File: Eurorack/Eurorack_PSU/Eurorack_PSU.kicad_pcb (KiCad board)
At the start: 2 copper layers, 95 x 58 mm, 20 parts, among them J1 AC, J2 AC, U1 LM7812_TO220, U2 LM7912_TO220

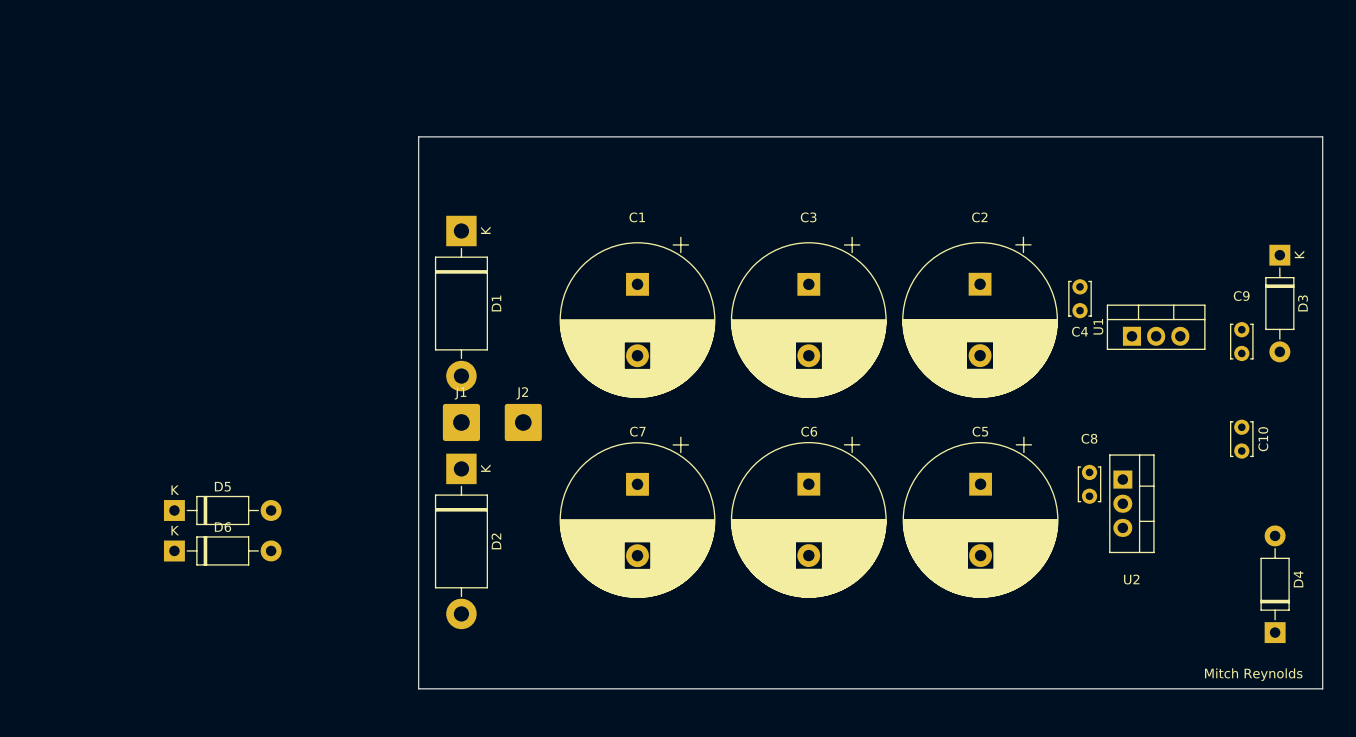
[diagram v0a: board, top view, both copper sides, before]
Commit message: Update PSU and add more spice models
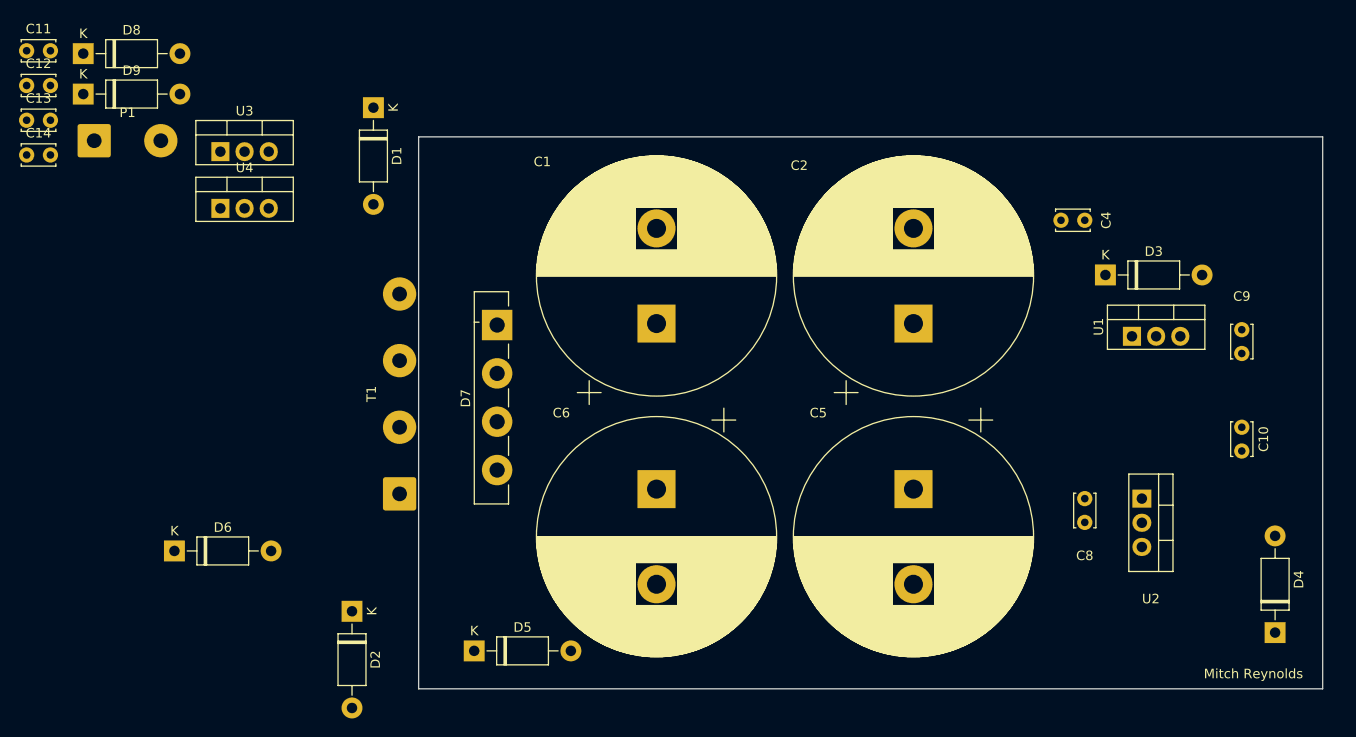
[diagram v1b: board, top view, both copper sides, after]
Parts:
- removed C3, C7: 2200uF 25v, Capacitor_THT:CP_Radial_D16.0mm_P7.50mm
- removed J1, J2: AC, Connector_Wire:SolderWire-1sqmm_1x01_D1.4mm_OD3.9mm
- added C11: 1uF, Capacitor_THT:C_Disc_D3.4mm_W2.1mm_P2.50mm, F.Cu at (14.8, 25.9)
- added C12: 1uF, Capacitor_THT:C_Disc_D3.4mm_W2.1mm_P2.50mm, F.Cu at (14.8, 29.6)
- added C13: 1uF, Capacitor_THT:C_Disc_D3.4mm_W2.1mm_P2.50mm, F.Cu at (14.8, 33.2)
- added C14: 1uF, Capacitor_THT:C_Disc_D3.4mm_W2.1mm_P2.50mm, F.Cu at (14.8, 36.9)
- added D7: GBU6A, Diode_THT:Diode_Bridge_Vishay_GBU, F.Cu at (64.2, 54.8)
- added D8: 1N4007, Diode_THT:D_DO-41_SOD81_P10.16mm_Horizontal, F.Cu at (20.8, 26.2)
- added D9: 1N4007, Diode_THT:D_DO-41_SOD81_P10.16mm_Horizontal, F.Cu at (20.8, 30.5)
- added P1: 240VAC 50Hz, Connector_Wire:SolderWire-0.75sqmm_1x02_P7mm_D1.25mm_OD3.5mm, F.Cu at (21.9, 35.4)
- added T1: 20:1, Connector_Wire:SolderWire-0.75sqmm_1x04_P7mm_D1.25mm_OD3.5mm, F.Cu at (54.0, 72.5)
- added U3: LM7805, Package_TO_SOT_THT:TO-220-3_Vertical, F.Cu at (35.2, 36.5)
- added U4: LM7905, Package_TO_SOT_THT:TO-220-3_Vertical, F.Cu at (35.2, 42.5)
- C1, C2, C5, C6: value 2200uF 25v -> 10000uF; footprint Capacitor_THT:CP_Radial_D16.0mm_P7.50mm -> Capacitor_THT:CP_Radial_D25.0mm_P10.00mm_SnapIn
- C10, C4, C8: value 1uf 50v -> 1uF
- C9: value 1uf -> 1uF
- D1, D2: value 1N5822 -> 1N4007; footprint Diode_THT:D_DO-201AD_P15.24mm_Horizontal -> Diode_THT:D_DO-41_SOD81_P10.16mm_Horizontal
- U1: value LM7812_TO220 -> LM7812
- U2: value LM7912_TO220 -> LM7912
- moved D5 34.8 mm to (61.8, 89.0)
- moved D2 18.9 mm to (49.0, 84.8)
- moved D3 18.4 mm to (128.2, 49.5), turned to 0 degrees
- moved C6 16.0 mm to (81.0, 72.0)
- moved D1 15.9 mm to (51.2, 31.9)
- moved C2 8.13 mm to (108.0, 54.6), turned to 90 degrees
- moved C4 7.28 mm to (123.5, 43.8), turned to 0 degrees
- moved C5 7.07 mm to (108.0, 72.0)
- moved C8 5.27 mm to (126.0, 75.5), turned to 90 degrees
- moved C1 4.58 mm to (81.0, 54.6), turned to 90 degrees
- moved U2 2.83 mm to (132.0, 73.0)
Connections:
- net Net-(D1-A) renamed +5V
- C1 pad 2: GND -> 0
- C10 pad 1: Net-(C10-Pad1) -> -12V
- C10 pad 2: -12V -> 0
- C2 pad 2: GND -> 0
- C4 pad 2: GND -> 0
- C5 pad 1: GND -> 0
- C5 pad 2: Net-(D2-A) -> Net-(D4-A)
- C6 pad 1: GND -> 0
- C6 pad 2: Net-(D2-A) -> Net-(D4-A)
- C8 pad 1: GND -> Net-(D4-A)
- C8 pad 2: Net-(D2-A) -> 0
- C9 pad 2: Net-(C10-Pad1) -> 0
- D2 pad 2: Net-(D2-A) -> 0
- D4 pad 2: Net-(D2-A) -> Net-(D4-A)
- D5 pad 2: GND -> 0
- D6 pad 1: GND -> 0
- U1 pad 2: GND -> 0
- U2 pad 1: GND -> 0
- U2 pad 2: Net-(D2-A) -> Net-(D4-A)
